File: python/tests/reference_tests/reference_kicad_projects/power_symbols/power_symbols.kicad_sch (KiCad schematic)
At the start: 2 parts

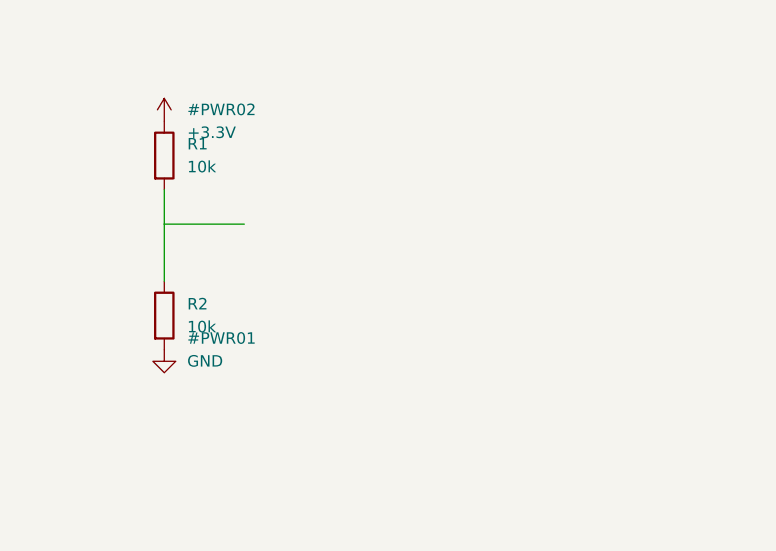
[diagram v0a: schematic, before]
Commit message: feat: Implement professional power symbol generation with proper formatting
## Power Symbol Enhancements
- **Hidden reference designators** - Power symbol references (#PWR01, #PWR02, etc.) now hidden by default
- **Correct value positioning** - Power symbol values positioned according to KiCAD conventions:
  - +3.3V and VDD values above symbols
  - GND values below symbols
  - Proper spacing and alignment

## Implementation Features
- **Automatic power symbol detection** via 'power:' lib_id prefix
- **Custom value property method** for power-specific positioning
- **Reference hiding** for clean schematic appearance
- **Professional formatting** matching KiCAD native output

## Test Coverage
- **test_power_symbols.py** demonstrates three power symbol types
- **Positions match reference** project exactly
- **Test runner integration** with validation for 3 power symbols
- **Content verification** for lib_ids and hidden references

## Generated Output
Creates clean, professional schematics with:
- power:+3.3V at (78.74, 64.77) - #PWR01
- power:GND at (154.94, 69.85) - #PWR02
- power:VDD at (113.03, 115.57) - #PWR03

All power symbols display correctly in KiCAD with proper symbol graphics and hidden references.

🤖 Generated with Claude Code

Co-Authored-By: Claude <noreply@anthropic.com>
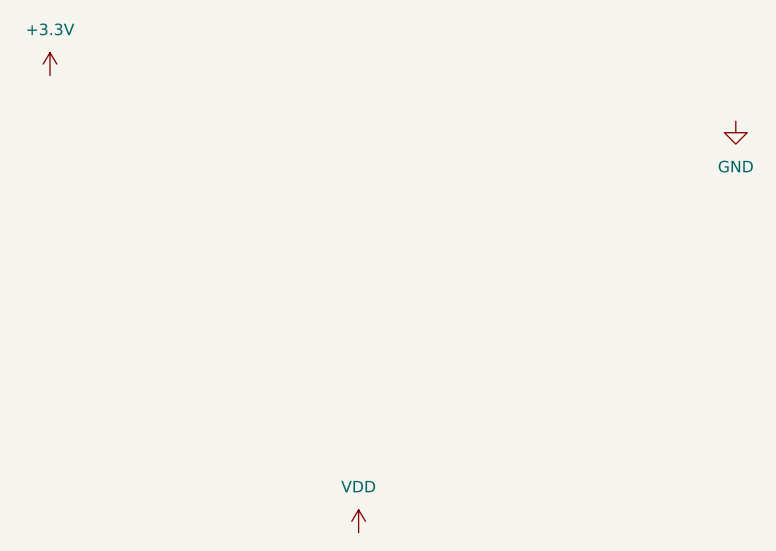
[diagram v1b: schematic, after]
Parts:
- removed R1, R2: 10k, Resistor_SMD:R_0603_1608Metric, symbol Device:R
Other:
- title: Resistor Divider -> (none)
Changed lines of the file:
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@@
 	(version 20250114)
 	(generator "eeschema")
-	(generator_version 9.0)
-	(paper A4)
-	(title_block
-		(title "Resistor Divider")
-	)
+	(generator_version "9.0")
+	(paper "A4")
 	(symbol
-		(lib_id "power:+3.3V")
-		(at 91.44 69.85 0)
+		(lib_id "power:GND")
+		(at 154.94 69.85 0)
 		(unit 1)
 		(exclude_from_sim no)
@@
 		(fields_autoplaced yes)
 		(property "Reference" "#PWR02"
-			(at 93.98 68.58 0)
-			(effects
-				(font
-					(size 1.27 1.27)
-				)
-				(justify left)
-			)
-		)
-		(property "Value" "+3.3V"
-			(at 93.98 71.12 0)
-			(effects
-				(font
-					(size 1.27 1.27)
-				)
-				(justify left)
+			(at 154.94 76.2 0)
+			(effects
+				(font
+					(size 1.27 1.27)
+				)
+				(hide yes)
+			)
+		)
+		(property "Value" "GND"
+			(at 154.94 74.93 0)
+			(effects
+				(font
+					(size 1.27 1.27)
+				)
 			)
 		)
 		(property "Footprint" ""
-			(at 93.98 73.66 0)
-			(effects
-				(font
-					(size 1.27 1.27)
-				)
-				(justify left)
-				(hide yes)
-			)
-		)
-		(property "datasheet" ""
-			(at 93.98 74.93 0)
-			(effects
-				(font
-					(size 1.27 1.27)
-				)
-				(justify left)
-				(hide yes)
-			)
-		)
-		(property "description" "Power symbol creates a global label with name +3.3V"
-			(at 93.98 74.93 0)
-			(effects
-				(font
-					(size 1.27 1.27)
-				)
-				(justify left)
+			(at 154.94 69.85 0)
+			(effects
+				(font
+					(size 1.27 1.27)
+				)
+				(hide yes)
+			)
+		)
+		(property "Datasheet" ""
+			(at 154.94 69.85 0)
+			(effects
+				(font
+					(size 1.27 1.27)
+				)
+				(hide yes)
+			)
+		)
+		(property "Description" "Power symbol creates a global label with name \"GND\" , ground"
+			(at 154.94 69.85 0)
+			(effects
+				(font
+					(size 1.27 1.27)
+				)
 				(hide yes)
 			)
@@
 		)
 		(instances
-			(project "simple_circuit"
-				(path "/dc573442-1a5c-4aaa-9ded-0bfcd2a9ad64"
+			(project ""
+				(path "/81a52d2e-122b-4a87-8546-0564d52bc16d"
 					(reference "#PWR02")
 					(unit 1)
@@
 	)
 	(symbol
-		(lib_id "power:GND")
-		(at 91.44 95.25 0)
+		(lib_id "power:VDD")
+		(at 113.03 115.57 0)
+		(unit 1)
+		(exclude_from_sim no)
+		(in_bom yes)
+		(on_board yes)
+		(dnp no)
+		(fields_autoplaced yes)
+		(property "Reference" "#PWR03"
+			(at 113.03 119.38 0)
+			(effects
+				(font
+					(size 1.27 1.27)
+				)
+				(hide yes)
+			)
+		)
+		(property "Value" "VDD"
+			(at 113.03 110.49 0)
+			(effects
+				(font
+					(size 1.27 1.27)
+				)
+			)
+		)
+		(property "Footprint" ""
+			(at 113.03 115.57 0)
+			(effects
+				(font
+					(size 1.27 1.27)
+				)
+				(hide yes)
+			)
+		)
+		(property "Datasheet" ""
+			(at 113.03 115.57 0)
+			(effects
+				(font
+					(size 1.27 1.27)
+				)
+				(hide yes)
+			)
+		)
+		(property "Description" "Power symbol creates a global label with name \"VDD\""
+			(at 113.03 115.57 0)
+			(effects
+				(font
+					(size 1.27 1.27)
+				)
+				(hide yes)
+			)
+		)
+		(pin "1"
+		)
+		(instances
+			(project ""
+				(path "/81a52d2e-122b-4a87-8546-0564d52bc16d"
+					(reference "#PWR03")
+					(unit 1)
+				)
+			)
+		)
+	)
+	(symbol
+		(lib_id "power:+3.3V")
+		(at 78.74 64.77 0)
 		(unit 1)
 		(exclude_from_sim no)
@@
 		(fields_autoplaced yes)
 		(property "Reference" "#PWR01"
-			(at 93.98 93.98 0)
-			(effects
-				(font
-					(size 1.27 1.27)
-				)
-				(justify left)
-			)
-		)
-		(property "Value" "GND"
-			(at 93.98 96.52 0)
-			(effects
-				(font
-					(size 1.27 1.27)
-				)
-				(justify left)
+			(at 78.74 68.58 0)
+			(effects
+				(font
+					(size 1.27 1.27)
+				)
+				(hide yes)
+			)
+		)
+		(property "Value" "+3.3V"
+			(at 78.74 59.69 0)
+			(effects
+				(font
+					(size 1.27 1.27)
+				)
 			)
 		)
 		(property "Footprint" ""
-			(at 93.98 99.06 0)
-			(effects
-				(font
-					(size 1.27 1.27)
-				)
-				(justify left)
-				(hide yes)
-			)
-		)
-		(property "datasheet" ""
-			(at 93.98 100.33 0)
-			(effects
-				(font
-					(size 1.27 1.27)
-				)
-				(justify left)
-				(hide yes)
-			)
-		)
-		(property "description" "Power symbol creates a global label with name GND, ground"
-			(at 93.98 100.33 0)
-			(effects
-				(font
-					(size 1.27 1.27)
-				)
-				(justify left)
+			(at 78.74 64.77 0)
+			(effects
+				(font
+					(size 1.27 1.27)
+				)
+				(hide yes)
+			)
+		)
+		(property "Datasheet" ""
+			(at 78.74 64.77 0)
+			(effects
+				(font
+					(size 1.27 1.27)
+				)
+				(hide yes)
+			)
+		)
+		(property "Description" "Power symbol creates a global label with name \"+3.3V\""
+			(at 78.74 64.77 0)
+			(effects
+				(font
+					(size 1.27 1.27)
+				)
 				(hide yes)
 			)
@@
 		)
 		(instances
-			(project "simple_circuit"
-				(path "/dc573442-1a5c-4aaa-9ded-0bfcd2a9ad64"
+			(project ""
+				(path "/81a52d2e-122b-4a87-8546-0564d52bc16d"
 					(reference "#PWR01")
 					(unit 1)
 				)
 			)
-		)
-	)
-	(symbol
-		(lib_id "Device:R")
-		(at 91.44 73.66 0)
-		(unit 1)
-		(exclude_from_sim no)
-		(in_bom yes)
-		(on_board yes)
-		(dnp no)
-		(fields_autoplaced yes)
-		(property "Reference" "R1"
-			(at 93.98 72.39 0)
-			(effects
-				(font
-					(size 1.27 1.27)
-				)
-				(justify left)
-			)
-		)
-		(property "Value" "10k"
-			(at 93.98 74.93 0)
-			(effects
-				(font
-					(size 1.27 1.27)
-				)
-				(justify left)
-			)
-		)
-		(property "Footprint" "Resistor_SMD:R_0603_1608Metric"
-			(at 93.98 77.47 0)
-			(effects
-				(font
-					(size 1.27 1.27)
-				)
-				(justify left)
-				(hide yes)
-			)
-		)
-		(property "datasheet" "~"
-			(at 93.98 78.74 0)
-			(effects
-				(font
-					(size 1.27 1.27)
-				)
-				(justify left)
-				(hide yes)
-			)
-		)
-		(property "description" "Resistor"
-			(at 93.98 78.74 0)
-			(effects
-				(font
-					(size 1.27 1.27)
-				)
-				(justify left)
-				(hide yes)
-			)
-		)
-		(pin "1"
-		)
-		(pin "2"
-		)
-		(instances
-			(project "simple_circuit"
-				(path "/dc573442-1a5c-4aaa-9ded-0bfcd2a9ad64"
-					(reference "R1")
-					(unit 1)
-				)
-			)
-		)
-	)
-	(symbol
-		(lib_id "Device:R")
-		(at 91.44 91.44 0)
-		(unit 1)
-		(exclude_from_sim no)
-		(in_bom yes)
-		(on_board yes)
-		(dnp no)
-		(fields_autoplaced yes)
-		(property "Reference" "R2"
-			(at 93.98 90.17 0)
-			(effects
-				(font
-					(size 1.27 1.27)
-				)
-				(justify left)
-			)
-		)
-		(property "Value" "10k"
-			(at 93.98 92.71 0)
-			(effects
-				(font
-					(size 1.27 1.27)
-				)
-				(justify left)
-			)
-		)
-		(property "Footprint" "Resistor_SMD:R_0603_1608Metric"
-			(at 93.98 95.25 0)
-			(effects
-				(font
-					(size 1.27 1.27)
-				)
-				(justify left)
-				(hide yes)
-			)
-		)
-		(property "datasheet" "~"
-			(at 93.98 96.52 0)
-			(effects
-				(font
-					(size 1.27 1.27)
-				)
-				(justify left)
-				(hide yes)
-			)
-		)
-		(property "description" "Resistor"
-			(at 93.98 96.52 0)
-			(effects
-				(font
-					(size 1.27 1.27)
-				)
-				(justify left)
-				(hide yes)
-			)
-		)
-		(pin "1"
-		)
-		(pin "2"
-		)
-		(instances
-			(project "simple_circuit"
-				(path "/dc573442-1a5c-4aaa-9ded-0bfcd2a9ad64"
-					(reference "R2")
-					(unit 1)
-				)
-			)
-		)
-	)
-	(wire
-		(pts
-			(xy 100.33 81.28)
-			(xy 91.44 81.28)
-		)
-		(stroke
-			(width 0)
-			(type default)
-		)
-	)
-	(wire
-		(pts
-			(xy 91.44 81.28)
-			(xy 91.44 77.47)
-		)
-		(stroke
-			(width 0)
-			(type default)
-		)
-	)
-	(wire
-		(pts
-			(xy 91.44 87.63)
-			(xy 91.44 81.28)
-		)
-		(stroke
-			(width 0)
-			(type default)
 		)
 	)
@@
 		)
 	)
-	(symbol_instances)
 	(embedded_fonts no)
 )
